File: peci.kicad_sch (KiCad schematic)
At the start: 10 parts, among them Q1401 PJE138K, U1401 MAX6621AUBT

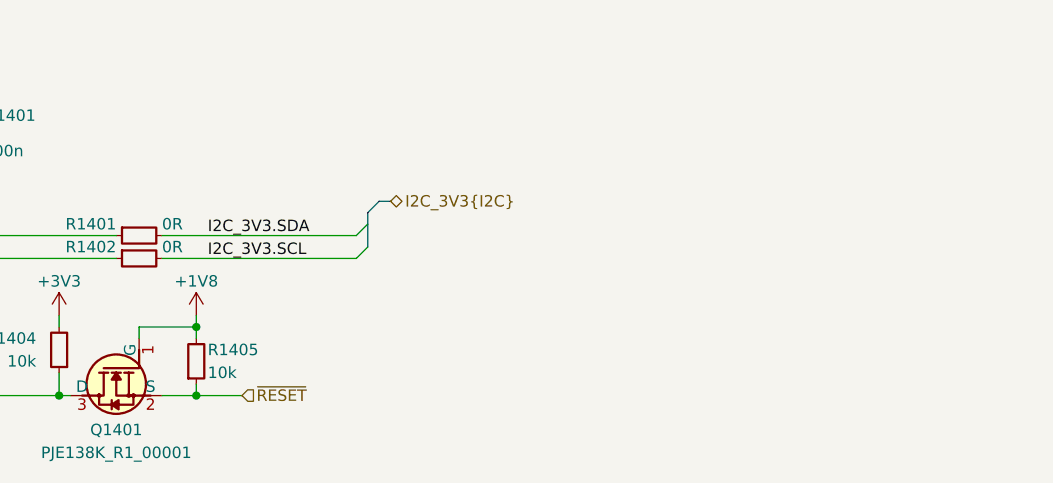
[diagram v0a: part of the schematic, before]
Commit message: [#100282] Swap TMP default from QSPI to SPI, add level shifter for PECI I2C bus, connect user button
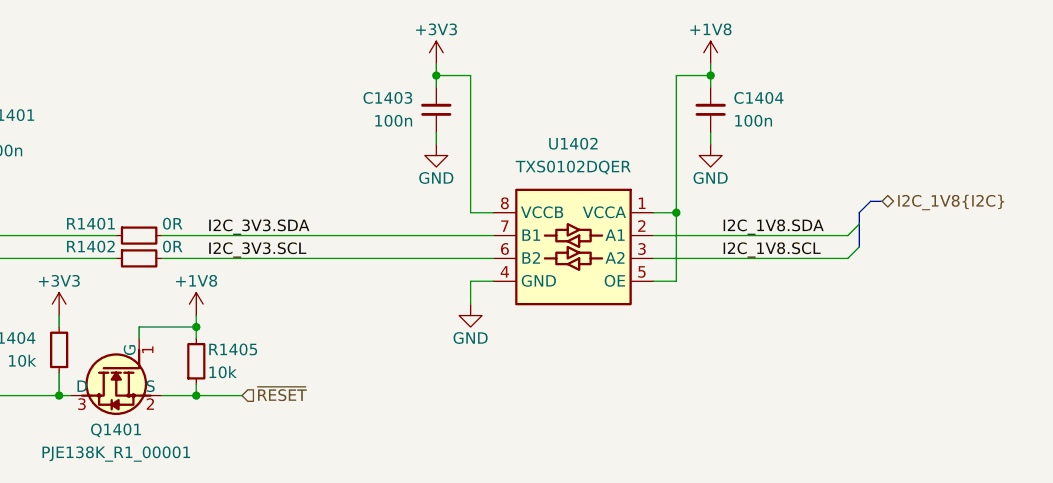
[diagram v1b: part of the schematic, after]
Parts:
- added C1403, C1404: C_100n_0402, antmicro-footprints:C_0402_1005Metric, symbol antmicroCapacitors0402:C_100n_0402
- added U1402: TXS0102DQER, antmicro-footprints:X2SON8_1.4x1x0.32mm_P0.35mm, symbol antmicroLogicTranslatorsLevelShifters:TXS0102DQER
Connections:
- net +1V8: now also C1404.2, U1402.1 (VCCA), U1402.5 (OE)
- net +3V3: now also C1403.2, U1402.8 (VCCB)
- net GND: now also C1403.1, C1404.1, U1402.4 (GND)
- net I2C_3V3.SCL: now also U1402.6 (B2)
- net I2C_3V3.SDA: now also U1402.7 (B1)
- new net I2C_1V8.SCL: U1402.3 (A2)
- new net I2C_1V8.SDA: U1402.2 (A1)

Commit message: [#100282] Update components from library
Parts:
- removed U1401: MAX6621AUBT, antmicro-footprints:VSSOP-10_3x3mm_P0.5mm, symbol antmicroInterfaceControllers:MAX6621AUBT
- added U1401: MAX6621AUB, antmicro-footprints:VSSOP-10_3x3mm_P0.5mm, symbol antmicroInterfaceControllers:MAX6621AUB
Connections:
- net +3V3: now also U1401.6 (VCC)
- net DC_SCM_PECI: now also U1401.1 (PECI)
- net GND: now also U1401.2 (AGND), U1401.7 (GND)
- net PECI_VREF: now also U1401.10 (VREF)
- net SCL: now also U1401.5 (SCL)
- net SDA: now also U1401.4 (SDA)
- net at Q1401.3 (D), R1404.1: now also U1401.8 (~{RESET})
- net at TP1401.1: now also U1401.9 (~{ALERT})
- net at R1403.2: now also U1401.3 (AD0)
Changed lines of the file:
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@@
-	)
-	(symbol
-		(lib_id "antmicroInterfaceControllers:MAX6621AUBT")
-		(at 210.82 121.92 0)
-		(mirror y)
-		(unit 1)
-		(body_style 1)
-		(exclude_from_sim no)
-		(in_bom yes)
-		(on_board yes)
-		(in_pos_files yes)
-		(dnp no)
-		(fields_autoplaced yes)
-		(property "Reference" "U1401"
-			(at 199.39 114.3 0)
-			(show_name no)
-			(do_not_autoplace no)
-			(effects
-				(font
-					(size 1.27 1.27)
-					(thickness 0.15)
-				)
-			)
-		)
-		(property "Value" "MAX6621AUBT"
-			(at 175.26 129.54 0)
-			(hide yes)
-			(show_name no)
-			(do_not_autoplace no)
-			(effects
-				(font
-					(size 1.27 1.27)
-					(thickness 0.15)
-				)
-				(justify left bottom)
-			)
-		)
-		(property "Footprint" "antmicro-footprints:VSSOP-10_3x3mm_P0.5mm"
-			(at 175.26 132.08 0)
-			(hide yes)
-			(show_name no)
-			(do_not_autoplace no)
-			(effects
-				(font
-					(size 1.27 1.27)
-					(thickness 0.15)
-				)
-				(justify left bottom)
-			)
-		)
-		(property "Datasheet" "https://www.analog.com/media/en/technical-documentation/data-sheets/MAX6621.pdf"
-			(at 175.26 134.62 0)
-			(hide yes)
-			(show_name no)
-			(do_not_autoplace no)
-			(effects
-				(font
-					(size 1.27 1.27)
-					(thickness 0.15)
-				)
-				(justify left bottom)
-			)
-		)
-		(property "Description" "PECI to I2C translator, 400 kbps, Vin 3V - 3.6V"
-			(at 175.26 137.16 0)
-			(hide yes)
-			(show_name no)
-			(do_not_autoplace no)
-			(effects
-				(font
-					(size 1.27 1.27)
-					(thickness 0.15)
-				)
-				(justify left bottom)
-			)
-		)
-		(property "Manufacturer" "Analog Devices"
-			(at 175.26 139.7 0)
-			(hide yes)
-			(show_name no)
-			(do_not_autoplace no)
-			(effects
-				(font
-					(size 1.27 1.27)
-					(thickness 0.15)
-				)
-				(justify left bottom)
-			)
-		)
-		(property "MPN" "MAX6621AUB+"
-			(at 199.39 116.84 0)
-			(show_name no)
-			(do_not_autoplace no)
-			(effects
-				(font
-					(size 1.27 1.27)
-					(thickness 0.15)
-				)
-			)
-		)
-		(property "Author" "Antmicro"
-			(at 175.26 142.24 0)
-			(hide yes)
-			(show_name no)
-			(do_not_autoplace no)
-			(effects
-				(font
-					(size 1.27 1.27)
-					(thickness 0.15)
-				)
-				(justify left bottom)
-			)
-		)
-		(property "License" "Apache-2.0"
-			(at 175.26 144.78 0)
-			(hide yes)
-			(show_name no)
-			(do_not_autoplace no)
-			(effects
-				(font
-					(size 1.27 1.27)
-					(thickness 0.15)
-				)
-				(justify left bottom)
-			)
-		)
-		(pin "3"
-		)
-		(pin "6"
-		)
-		(pin "10"
-		)
-		(pin "1"
-		)
-		(pin "5"
-		)
-		(pin "4"
-		)
-		(pin "7"
-		)
-		(pin "2"
-		)
-		(pin "9"
-		)
-		(pin "8"
-		)
-		(instances
-			(project "altera-modular-agilex-5-dc-scm"
-				(path "/6bb9d978-a328-4b30-874b-55170a976185/b18fedc8-291b-45fb-9413-07ab4e9140fd"
-					(reference "U1401")
-					(unit 1)
-				)
-			)
-		)
 	)
 	(symbol
@@
 					(unit 1)
 				)
+			)
+		)
+	)
+	(symbol
+		(lib_id "antmicroInterfaceControllers:MAX6621AUB")
+		(at 210.82 121.92 0)
+		(mirror y)
+		(unit 1)
+		(body_style 1)
+		(exclude_from_sim no)
+		(in_bom yes)
+		(on_board yes)
+		(in_pos_files yes)
+		(dnp no)
+		(property "Reference" "U1401"
+			(at 199.39 114.3 0)
+			(show_name no)
+			(do_not_autoplace no)
+			(effects
+				(font
+					(size 1.27 1.27)
+					(thickness 0.15)
+				)
+			)
+		)
+		(property "Value" "MAX6621AUB"
+			(at 175.26 129.54 0)
+			(hide yes)
+			(show_name no)
+			(do_not_autoplace no)
+			(effects
+				(font
+					(size 1.27 1.27)
+					(thickness 0.15)
+				)
+				(justify left bottom)
+			)
+		)
+		(property "Footprint" "antmicro-footprints:VSSOP-10_3x3mm_P0.5mm"
+			(at 175.26 132.08 0)
+			(hide yes)
+			(show_name no)
+			(do_not_autoplace no)
+			(effects
+				(font
+					(size 1.27 1.27)
+					(thickness 0.15)
+				)
+				(justify left bottom)
+			)
+		)
+		(property "Datasheet" "https://www.analog.com/media/en/technical-documentation/data-sheets/MAX6621.pdf"
+			(at 175.26 134.62 0)
+			(hide yes)
+			(show_name no)
+			(do_not_autoplace no)
+			(effects
+				(font
+					(size 1.27 1.27)
+					(thickness 0.15)
+				)
+				(justify left bottom)
+			)
+		)
+		(property "Description" "PECI to I2C translator, 400 kbps, Vin 3V - 3.6V"
+			(at 175.26 137.16 0)
+			(hide yes)
+			(show_name no)
+			(do_not_autoplace no)
+			(effects
+				(font
+					(size 1.27 1.27)
+					(thickness 0.15)
+				)
+				(justify left bottom)
+			)
+		)
+		(property "Manufacturer" "Analog Devices"
+			(at 175.26 139.7 0)
+			(hide yes)
+			(show_name no)
+			(do_not_autoplace no)
+			(effects
+				(font
+					(size 1.27 1.27)
+					(thickness 0.15)
+				)
+				(justify left bottom)
+			)
+		)
+		(property "MPN" "MAX6621AUB+"
+			(at 199.39 116.84 0)
+			(show_name no)
+			(do_not_autoplace no)
+			(effects
+				(font
+					(size 1.27 1.27)
+					(thickness 0.15)
+				)
+			)
+		)
+		(property "Author" "Antmicro"
+			(at 175.26 142.24 0)
+			(hide yes)
+			(show_name no)
+			(do_not_autoplace no)
+			(effects
+				(font
+					(size 1.27 1.27)
+					(thickness 0.15)
+				)
+				(justify left bottom)
+			)
+		)
+		(property "License" "Apache-2.0"
+			(at 175.26 144.78 0)
+			(hide yes)
+			(show_name no)
+			(do_not_autoplace no)
+			(effects
+				(font
+					(size 1.27 1.27)
+					(thickness 0.15)
+				)
+				(justify left bottom)
+			)
+		)
+		(pin "7"
+		)
+		(pin "9"
+		)
+		(pin "10"
+		)
+		(pin "1"
+		)
+		(pin "6"
+		)
+		(pin "5"
+		)
+		(pin "3"
+		)
+		(pin "4"
+		)
+		(pin "8"
+		)
+		(pin "2"
+		)
+		(instances
+			(project "altera-modular-agilex-5-dc-scm"
+				(path "/6bb9d978-a328-4b30-874b-55170a976185/b18fedc8-291b-45fb-9413-07ab4e9140fd"
+					(reference "U1401")
+					(unit 1)
+				)

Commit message: [#100282] Fix overlaping graphics, add schematic sheet names on them
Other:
- note added: "PECI PHY"
- moved on the sheet: C1401, C1402, C1403, C1404, Q1401, R1401, R1402, R1403, R1404, R1405, TP1401, U1401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

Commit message: [#100282] Add 0R to PECI RESET signal
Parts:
- added R1406: R_0R_0402, antmicro-footprints:R_0402_1005Metric, symbol antmicroResistors0402:R_0R_0402
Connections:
- net ~{RESET}: now also R1406.2; no longer Q1401.2 (S), R1405.1
- new net: Q1401.2 (S), R1405.1, R1406.1
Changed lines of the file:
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@@
+	)
+	(junction
+		(at 215.9 157.48)
+		(diameter 0)
+		(color 0 0 0 0)
 	)
 	(junction
@@
 		(color 0 0 0 0)
 	)
-	(junction
-		(at 215.9 157.48)
-		(diameter 0)
-		(color 0 0 0 0)
-	)
 	(bus_entry
 		(at 289.56 140.97)
@@
 	(wire
 		(pts
+			(xy 229.87 157.48) (xy 237.49 157.48)
+		)
+		(stroke
+			(width 0)
+			(type default)
+		)
+	)
+	(wire
+		(pts
 			(xy 212.09 142.24) (xy 248.92 142.24)
 		)
@@
 	(wire
 		(pts
-			(xy 215.9 157.48) (xy 220.98 157.48)
+			(xy 215.9 157.48) (xy 224.79 157.48)
 		)
 		(stroke
@@
 	(hierarchical_label "~{RESET}"
 		(shape input)
-		(at 220.98 157.48 0)
+		(at 237.49 157.48 0)
 		(effects
 			(font
@@
 					(unit 1)
 				)
+			)
+		)
+	)
+	(symbol
+		(lib_id "antmicroResistors0402:R_0R_0402")
+		(at 224.79 157.48 0)
+		(unit 1)
+		(body_style 1)
+		(exclude_from_sim no)
+		(in_bom yes)
+		(on_board yes)
+		(in_pos_files yes)
+		(dnp no)
+		(property "Reference" "R1406"
+			(at 229.87 156.21 0)
+			(show_name no)
+			(do_not_autoplace no)
+			(effects
+				(font
+					(size 1.27 1.27)
+					(thickness 0.15)
+				)
+				(justify left)
+			)
+		)
+		(property "Value" "R_0R_0402"
+			(at 245.11 170.18 0)
+			(hide yes)
+			(show_name no)
+			(do_not_autoplace no)
+			(effects
+				(font
+					(size 1.27 1.27)
+					(thickness 0.15)
+				)
+				(justify left bottom)
+			)
+		)
+		(property "Footprint" "antmicro-footprints:R_0402_1005Metric"
+			(at 245.11 172.72 0)
+			(hide yes)
+			(show_name no)
+			(do_not_autoplace no)
+			(effects
+				(font
+					(size 1.27 1.27)
+					(thickness 0.15)
+				)
+				(justify left bottom)
+			)
+		)
+		(property "Datasheet" "https://industrial.panasonic.com/cdbs/www-data/pdf/RDA0000/AOA0000C301.pdf"
+			(at 245.11 175.26 0)
+			(hide yes)
+			(show_name no)
+			(do_not_autoplace no)
+			(effects
+				(font
+					(size 1.27 1.27)
+					(thickness 0.15)
+				)
+				(justify left bottom)
+			)
+		)
+		(property "Description" "SMD Chip Resistor, Jumper, 0 ohm, 100 mW, 0402 [1005 Metric], Thick Film, General Purpose"
+			(at 224.79 157.48 0)
+			(hide yes)
+			(show_name no)
+			(do_not_autoplace no)
+			(effects
+				(font
+					(size 1.27 1.27)
+				)
+			)
+		)
+		(property "MPN" "ERJ2GE0R00X"
+			(at 245.11 177.8 0)
+			(hide yes)
+			(show_name no)
+			(do_not_autoplace no)
+			(effects
+				(font
+					(size 1.27 1.27)
+					(thickness 0.15)
+				)
+				(justify left bottom)
+			)
+		)
+		(property "Manufacturer" "Panasonic"
+			(at 245.11 180.34 0)
+			(hide yes)
+			(show_name no)
+			(do_not_autoplace no)
+			(effects
+				(font
+					(size 1.27 1.27)
+					(thickness 0.15)
+				)
+				(justify left bottom)
+			)
+		)
+		(property "License" "Apache-2.0"
+			(at 245.11 182.88 0)
+			(hide yes)
+			(show_name no)
+			(do_not_autoplace no)
+			(effects
+				(font
+					(size 1.27 1.27)
+					(thickness 0.15)
+				)
+				(justify left bottom)
+			)
+		)
+		(property "Author" "Antmicro"
+			(at 245.11 185.42 0)
+			(hide yes)
+			(show_name no)
+			(do_not_autoplace no)
+			(effects
+				(font
+					(size 1.27 1.27)
+					(thickness 0.15)
+				)
+				(justify left bottom)
+			)
+		)
+		(property "Val" "0R"
+			(at 224.79 156.21 0)
+			(show_name no)
+			(do_not_autoplace no)
+			(effects
+				(font
+					(size 1.27 1.27)
+					(thickness 0.15)
+				)
+				(justify right)
+			)
+		)
+		(property "Tolerance" ""
+			(at 245.11 167.64 0)
+			(hide yes)
+			(show_name no)
+			(do_not_autoplace no)
+			(effects
+				(font
+					(size 1.27 1.27)
+				)
+				(justify left bottom)
+			)
+		)
+		(property "Current" "1A"
+			(at 245.11 187.96 0)
+			(hide yes)
+			(show_name no)
+			(do_not_autoplace no)
+			(effects
+				(font
+					(size 1.27 1.27)
+					(thickness 0.15)
+				)
+				(justify left bottom)
+			)
+		)
+		(pin "1"
+		)
+		(pin "2"
+		)
+		(instances
+			(project "altera-modular-agilex-5-dc-scm"
+				(path "/6bb9d978-a328-4b30-874b-55170a976185/b18fedc8-291b-45fb-9413-07ab4e9140fd"
+					(reference "R1406")
+					(unit 1)
+				)
